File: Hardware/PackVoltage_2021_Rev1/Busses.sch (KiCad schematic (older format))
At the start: 10 parts

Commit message: added power input and buck converter subsheets
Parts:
- added D?: LED, symbol Device:LED
- added R?: R, symbol Device:R
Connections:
- net GND: now also R?.2
- net at Q?.3 (S), R?.1, U?.3 (+): now also D?.2 (A)
- new net: D?.1 (K), R?.1
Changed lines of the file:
@@
 $Descr A4 11693 8268
 encoding utf-8
-Sheet 3 3
+Sheet 3 5
 Title ""
 Date ""
@@
 Motor 1
 Wire Wire Line
-	3250 1850 3500 1850
-Wire Wire Line
 	3500 1850 3500 1450
 $Comp
@@
 	0    -1   -1   0
 $EndComp
+$Comp
+L Device:LED D?
+U 1 1 5F846899
+P 3350 2250
+F 0 "D?" H 3343 1995 50  0000 C CNN
+F 1 "LED" H 3343 2086 50  0000 C CNN
+F 2 "" H 3350 2250 50  0001 C CNN
+F 3 "~" H 3350 2250 50  0001 C CNN
+	1    3350 2250
+	0    -1   -1   0
+$EndComp
+Wire Wire Line
+	3250 1850 3350 1850
+Wire Wire Line
+	3350 1850 3350 2100
+Connection ~ 3350 1850
+Wire Wire Line
+	3350 1850 3500 1850
+$Comp
+L Device:R R?
+U 1 1 5F84DEAA
+P 3350 2700
+F 0 "R?" H 3420 2746 50  0000 L CNN
+F 1 "R" H 3420 2655 50  0000 L CNN
+F 2 "" V 3280 2700 50  0001 C CNN
+F 3 "~" H 3350 2700 50  0001 C CNN
+	1    3350 2700
+	1    0    0    -1
+$EndComp
+Wire Wire Line
+	3350 2400 3350 2550
+$Comp
+L power:GND #PWR?
+U 1 1 5F84F08B
+P 3350 2950
+F 0 "#PWR?" H 3350 2700 50  0001 C CNN
+F 1 "GND" H 3355 2777 50  0000 C CNN
+F 2 "" H 3350 2950 50  0001 C CNN
+F 3 "" H 3350 2950 50  0001 C CNN
+	1    3350 2950
+	1    0    0    -1
+$EndComp
+Wire Wire Line
+	3350 2850 3350 2950
 $EndSCHEMATC

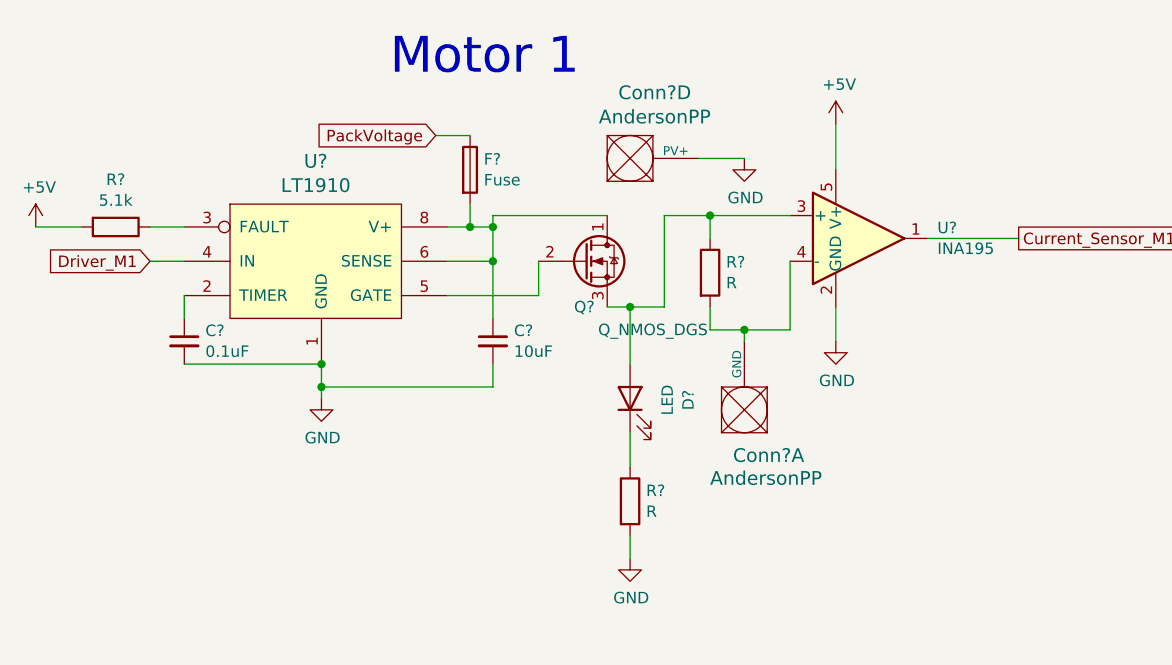
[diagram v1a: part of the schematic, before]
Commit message: added hierarchical labels, changed current sensor, added 12V labels to TIVA, finished buck sheet
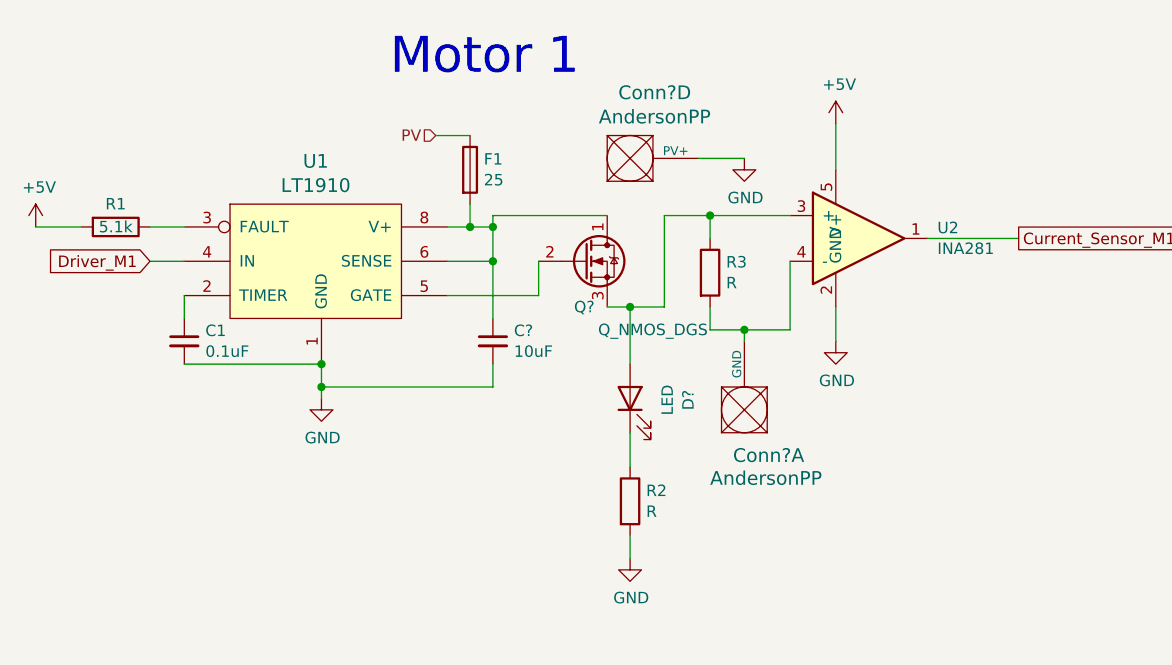
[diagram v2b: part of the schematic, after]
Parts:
- removed U?: LT1910, symbol MRDT_ICs:LT1910
- removed U?: INA195, Package_TO_SOT_SMD:SOT-23-5, symbol Amplifier_Current:INA195
- added U1: LT1910, symbol MRDT_ICs:LT1910
- added U2: INA281, symbol MRDT_ICs:INA281
- F1: renamed from F?; value Fuse -> 25
- gave numbers to parts that had none: 4
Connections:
- net +5V: now also U2.5 (V+)
- net Current_Sensor_M1: now also U2.1
- net Driver_M1: now also U1.4 (IN)
- net GND: now also U1.1 (GND), U2.2 (GND)
- net at C?.1, F1.2, Q?.1 (D): now also U1.6 (SENSE), U1.8 (V+)
- net at Q?.2 (G): now also U1.5 (GATE)
- net at D?.2 (A), Q?.3 (S), R3.1: now also U2.3 (+)
- net at C1.1: now also U1.2 (TIMER)
- net at R1.1: now also U1.3 (FAULT)
- net at Conn?.1 (GND), R3.2: now also U2.4 (-)
- net PackVoltage renamed PV
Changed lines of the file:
@@
-$EndComp
-$Comp
-L MRDT_ICs:LT1910 U?
-U 1 1 5F76B064
-P 1600 1900
-F 0 "U?" H 1975 2587 60  0000 C CNN
-F 1 "LT1910" H 1975 2481 60  0000 C CNN
-F 2 "" H 1600 1900 60  0001 C CNN
-F 3 "" H 1600 1900 60  0001 C CNN
-	1    1600 1900
-	1    0    0    -1
 $EndComp
 $Comp
@@
 	2000 2100 2000 2200
 $Comp
-L Device:Fuse F?
+L Device:Fuse F1
 U 1 1 5F78099C
 P 2650 1250
-F 0 "F?" H 2710 1296 50  0000 L CNN
-F 1 "Fuse" H 2710 1205 50  0000 L CNN
+F 0 "F1" H 2710 1296 50  0000 L CNN
+F 1 "25" H 2710 1205 50  0000 L CNN
 F 2 "" V 2580 1250 50  0001 C CNN
 F 3 "~" H 2650 1250 50  0001 C CNN
@@
 $EndComp
 $Comp
-L Device:R R?
+L Device:R R1
 U 1 1 5F78141C
 P 1100 1500
-F 0 "R?" V 893 1500 50  0000 C CNN
-F 1 "5.1k" V 984 1500 50  0000 C CNN
+F 0 "R1" V 1000 1500 50  0000 C CNN
+F 1 "5.1k" V 1100 1500 50  0000 C CNN
 F 2 "" V 1030 1500 50  0001 C CNN
 F 3 "~" H 1100 1500 50  0001 C CNN
@@
 	1250 1500 1400 1500
 $Comp
-L Device:C_Small C?
+L Device:C_Small C1
 U 1 1 5F7BBB24
 P 1400 2000
-F 0 "C?" H 1492 2046 50  0000 L CNN
+F 0 "C1" H 1492 2046 50  0000 L CNN
 F 1 "0.1uF" H 1492 1955 50  0000 L CNN
 F 2 "" H 1400 2000 50  0001 C CNN
@@
 Wire Wire Line
 	1400 2100 2000 2100
-Connection ~ 2000 2100
 $Comp
 L Device:C_Small C?
@@
 Wire Wire Line
 	2500 1100 2650 1100
-Text GLabel 2500 1100 0    50   Input ~ 0
-PackVoltage
 Wire Wire Line
 	2950 1800 2950 1650
@@
 	4050 1950 4050 1650
 $Comp
-L Device:R R?
+L Device:R R3
 U 1 1 5F7BF294
 P 3700 1700
-F 0 "R?" H 3770 1746 50  0000 L CNN
+F 0 "R3" H 3770 1746 50  0000 L CNN
 F 1 "R" H 3770 1655 50  0000 L CNN
 F 2 "" V 3630 1700 50  0001 C CNN
@@
 F 3 "" H 4250 1050 50  0001 C CNN
 	1    4250 1050
-	1    0    0    -1
-$EndComp
-$Comp
-L Amplifier_Current:INA195 U?
-U 1 1 5F76DF77
-P 4350 1550
-F 0 "U?" H 4694 1596 50  0000 L CNN
-F 1 "INA195" H 4694 1505 50  0000 L CNN
-F 2 "Package_TO_SOT_SMD:SOT-23-5" H 4350 1550 50  0001 C CNN
-F 3 "http://www.ti.com/lit/ds/symlink/ina193.pdf" H 4350 1550 50  0001 C CNN
-	1    4350 1550
 	1    0    0    -1
 $EndComp
@@
 	3350 1850 3500 1850
 $Comp
-L Device:R R?
+L Device:R R2
 U 1 1 5F84DEAA
 P 3350 2700
-F 0 "R?" H 3420 2746 50  0000 L CNN
+F 0 "R2" H 3420 2746 50  0000 L CNN
 F 1 "R" H 3420 2655 50  0000 L CNN
 F 2 "" V 3280 2700 50  0001 C CNN
@@
 Wire Wire Line
 	3350 2850 3350 2950
+Text HLabel 2500 1100 0    50   Input ~ 0
+PV
+$Comp
+L MRDT_ICs:INA281 U2
+U 1 1 5F8DF453
+P 4250 1550
+F 0 "U2" H 4694 1596 50  0000 L CNN
+F 1 "INA281" H 4694 1505 50  0000 L CNN
+F 2 "" H 4500 1750 50  0001 C CNN
+F 3 "" H 4500 1750 50  0001 C CNN
+	1    4250 1550
+	1    0    0    -1
+$EndComp
+$Comp
+L MRDT_ICs:LT1910 U1
+U 1 1 5F8E1128
+P 1600 1900
+F 0 "U1" H 1975 2587 60  0000 C CNN
+F 1 "LT1910" H 1975 2481 60  0000 C CNN
+F 2 "" H 1600 1900 60  0001 C CNN
+F 3 "" H 1600 1900 60  0001 C CNN
+	1    1600 1900
+	1    0    0    -1
+$EndComp
+Connection ~ 2000 2100
 $EndSCHEMATC
